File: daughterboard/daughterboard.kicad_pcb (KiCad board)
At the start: 2 copper layers, 45.7 x 56 mm, 39 parts, among them CON1 12V_JACK, IC1 ATMEGA328P-A, P1 X_PB01, P2 X_PC1, P3 CONN_13X2, P4 AZIMUTH, P5 ELEVATION, P6 X_ADC67, P7 VALVE, P8 X_PD4567, Q1 TIP120, U1 ULN2803A, Y1 8MHz

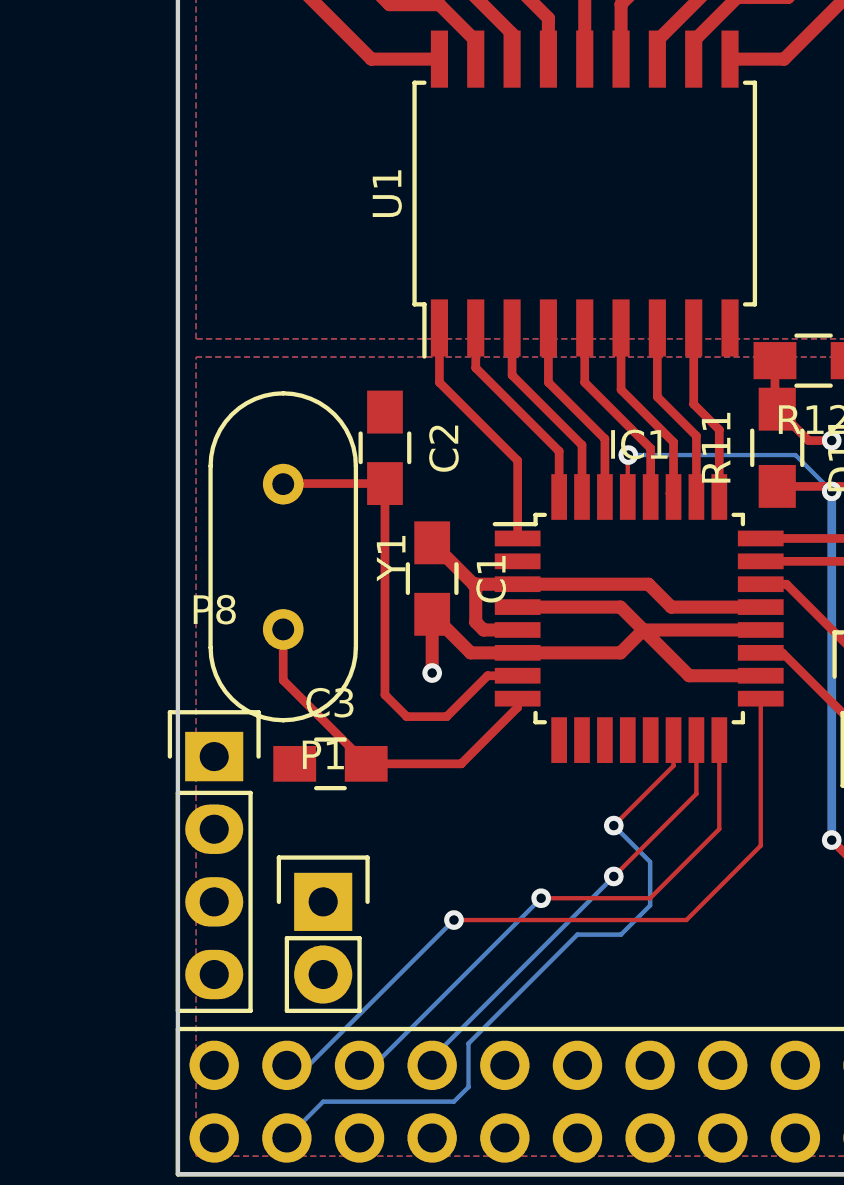
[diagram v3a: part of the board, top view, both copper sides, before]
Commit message: add GND->GNDD short resistor, connect X_PB01 but not X_PD4567
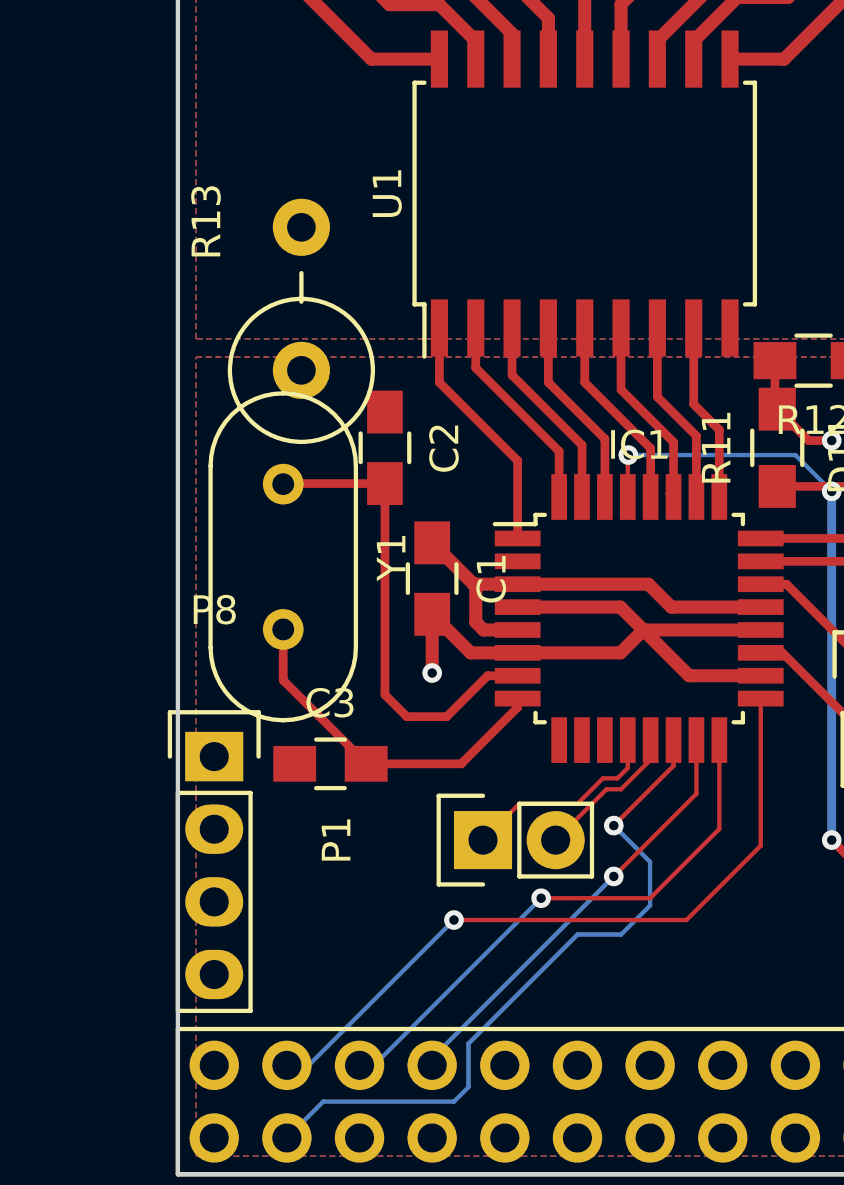
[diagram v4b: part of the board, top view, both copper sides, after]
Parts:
- added R13: SHORT, Resistors_ThroughHole:Resistor_Vertical_RM5mm, F.Cu at (147.8, 150.4)
- D10: value VALVE -> YELLOW
- D11: value RESET -> RED
- moved P1 5.99 mm to (154.2, 169.3), turned to 90 degrees
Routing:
- net Net-(IC1-Pad12): track 0.00 -> 7.08 mm
- net Net-(IC1-Pad13): track 0.00 -> 5.17 mm
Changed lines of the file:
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@@
 (kicad_pcb (version 4) (host pcbnew 4.0.2+dfsg1-stable)
   (general
-    (links 90)
-    (no_connects 9)
+    (links 92)
+    (no_connects 7)
     (area 143.424999 124.924999 189.295001 181.075001)
     (thickness 1.6)
     (drawings 37)
-    (tracks 186)
+    (tracks 196)
     (zones 0)
-    (modules 39)
+    (modules 40)
     (nets 50)
   )
@@
   )
   (setup
-    (last_trace_width 0.3048)
+    (last_trace_width 0.1524)
     (user_trace_width 0.1524)
     (user_trace_width 0.3048)
@@
       (effects (font (size 1 1) (thickness 0.15)))
     )
-    (fp_text value ATMEGA328P-A (at -0.381 6.223) (layer F.Fab)
+    (fp_text value ATMEGA328P-A (at -0.254 0.127) (layer F.Fab)
       (effects (font (size 1 1) (thickness 0.15)))
     )
@@
       (effects (font (size 1 1) (thickness 0.15)))
     )
-    (fp_text value 22pF (at 9.398 0) (layer F.Fab)
+    (fp_text value 22pF (at 4.572 -0.127) (layer F.Fab)
       (effects (font (size 1 1) (thickness 0.15)))
     )
@@
   )
   (module Pin_Headers:Pin_Header_Straight_1x02 (layer F.Cu)
-    (at 148.58 171.475)
+    (at 154.168 169.316 90)
     (descr "Through hole pin header")
     (tags "pin header")
-    (fp_text reference P1 (at 0 -5.1) (layer F.SilkS)
-      (effects (font (size 1 1) (thickness 0.15)))
-    )
-    (fp_text value X_PB01 (at 3.048 0.889 90) (layer F.Fab)
+    (fp_text reference P1 (at 0 -5.1 90) (layer F.SilkS)
+      (effects (font (size 1 1) (thickness 0.15)))
+    )
+    (fp_text value X_PB01 (at -1.397 -3.429 270) (layer F.Fab)
       (effects (font (size 1 1) (thickness 0.15)))
     )
@@
     (fp_line (start -1.27 1.27) (end -1.27 3.81) (layer F.SilkS) (width 0.15))
     (fp_line (start -1.27 3.81) (end 1.27 3.81) (layer F.SilkS) (width 0.15))
-    (pad 1 thru_hole rect (at 0 0) (size 2.032 2.032) (drill 1.016) (layers *.Cu *.Mask F.SilkS)
+    (pad 1 thru_hole rect (at 0 0 90) (size 2.032 2.032) (drill 1.016) (layers *.Cu *.Mask F.SilkS)
       (net 28 "Net-(IC1-Pad12)"))
-    (pad 2 thru_hole oval (at 0 2.54) (size 2.032 2.032) (drill 1.016) (layers *.Cu *.Mask F.SilkS)
+    (pad 2 thru_hole oval (at 0 2.54 90) (size 2.032 2.032) (drill 1.016) (layers *.Cu *.Mask F.SilkS)
       (net 29 "Net-(IC1-Pad13)"))
     (model Pin_Headers.3dshapes/Pin_Header_Straight_1x02.wrl
@@
       (effects (font (size 1 1) (thickness 0.15)))
     )
-    (fp_text value VALVE (at 1.905 -3.81) (layer F.Fab)
+    (fp_text value YELLOW (at 1.905 -3.81) (layer F.Fab)
       (effects (font (size 1 1) (thickness 0.15)))
     )
@@
       (effects (font (size 1 1) (thickness 0.15)))
     )
-    (fp_text value RESET (at -0.127 1.651 90) (layer F.Fab)
+    (fp_text value RED (at -0.127 1.651 90) (layer F.Fab)
       (effects (font (size 1 1) (thickness 0.15)))
     )
@@
       (rotate (xyz 0 0 90))
     )
+  )
+  (module Resistors_ThroughHole:Resistor_Vertical_RM5mm (layer F.Cu)
+    (at 147.818 150.393 90)
+    (descr "Resistor, Vertical, RM 5mm, 1/3W,")
+    (tags "Resistor, Vertical, RM 5mm, 1/3W,")
+    (fp_text reference R13 (at 2.70002 -3.29946 90) (layer F.SilkS)
+      (effects (font (size 1 1) (thickness 0.15)))
+    )
+    (fp_text value SHORT (at 0.381 -2.032 90) (layer F.Fab)
+      (effects (font (size 1 1) (thickness 0.15)))
+    )
+    (fp_line (start -0.09906 0) (end 0.9017 0) (layer F.SilkS) (width 0.15))
+    (fp_circle (center -2.49936 0) (end 0 0) (layer F.SilkS) (width 0.15))
+    (pad 1 thru_hole circle (at -2.49936 0 90) (size 1.99898 1.99898) (drill 1.00076) (layers *.Cu *.SilkS *.Mask)
+      (net 2 GNDD))
+    (pad 2 thru_hole circle (at 2.5019 0 90) (size 1.99898 1.99898) (drill 1.00076) (layers *.Cu *.SilkS *.Mask)
+      (net 1 GND))
   )
   (gr_line (start 189.22 125.12) (end 143.5 125.12) (angle 90) (layer Edge.Cuts) (width 0.15))
@@
   (segment (start 167.005 137.683) (end 167.005 137.16) (width 0.4572) (layer F.Cu) (net 23))
   (segment (start 167.005 134.39902) (end 167.005 137.16) (width 0.1524) (layer F.Cu) (net 23))
+  (segment (start 159.229 165.819) (end 159.229 166.795) (width 0.1524) (layer F.Cu) (net 28))
+  (segment (start 155.438 168.046) (end 154.168 169.316) (width 0.1524) (layer F.Cu) (net 28))
+  (segment (start 157.47 168.046) (end 155.438 168.046) (width 0.1524) (layer F.Cu) (net 28))
+  (segment (start 158.359 167.157) (end 157.47 168.046) (width 0.1524) (layer F.Cu) (net 28))
+  (segment (start 158.867 167.157) (end 158.359 167.157) (width 0.1524) (layer F.Cu) (net 28))
+  (segment (start 159.229 166.795) (end 158.867 167.157) (width 0.1524) (layer F.Cu) (net 28))
+  (segment (start 160.029 165.819) (end 160.029 166.503) (width 0.1524) (layer F.Cu) (net 29))
+  (segment (start 160.029 166.503) (end 158.994 167.538) (width 0.1524) (layer F.Cu) (net 29))
+  (segment (start 158.994 167.538) (end 158.486 167.538) (width 0.1524) (layer F.Cu) (net 29))
+  (segment (start 158.486 167.538) (end 156.708 169.316) (width 0.1524) (layer F.Cu) (net 29))
   (segment (start 147.31 179.73) (end 148.58 178.46) (width 0.1524) (layer B.Cu) (net 30))
   (segment (start 160.829 166.719) (end 160.829 165.819) (width 0.1524) (layer F.Cu) (net 30))
@@
   (segment (start 170.799 158.769) (end 171.44 159.41) (width 0.3048) (layer F.Cu) (net 37))
   (segment (start 170.799 158.769) (end 171.44 159.41) (width 0.1524) (layer F.Cu) (net 37))
-  (segment (start 167.63 177.19) (end 167.63 170.586) (width 0.3048) (layer F.Cu) (net 38) (status 400000))
+  (segment (start 167.63 177.19) (end 167.63 170.586) (width 0.3048) (layer F.Cu) (net 38))
   (segment (start 166.36 169.316) (end 166.36 157.124) (width 0.3048) (layer B.Cu) (net 38))
   (via (at 166.36 169.316) (size 0.6858) (drill 0.3302) (layers F.Cu B.Cu) (net 38))
   (segment (start 167.63 170.586) (end 166.36 169.316) (width 0.3048) (layer F.Cu) (net 38))
   (segment (start 166.36 156.95) (end 166.36 157.124) (width 0.1524) (layer F.Cu) (net 38))
-  (segment (start 159.229 155.873) (end 159.229 157.319) (width 0.1524) (layer F.Cu) (net 38) (status 800000))
+  (segment (start 159.229 155.873) (end 159.229 157.319) (width 0.1524) (layer F.Cu) (net 38))
   (segment (start 159.248 155.854) (end 159.229 155.873) (width 0.1524) (layer F.Cu) (net 38))
   (via (at 159.248 155.854) (size 0.6858) (drill 0.3302) (layers F.Cu B.Cu) (net 38))
